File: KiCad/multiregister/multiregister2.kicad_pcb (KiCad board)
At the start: 2 copper layers, 6 parts, among them K1 CONN_3, K2 CONN_3, P1 CONN_5, P2 CONN_8, P3 CONN_5, U1 74HC595

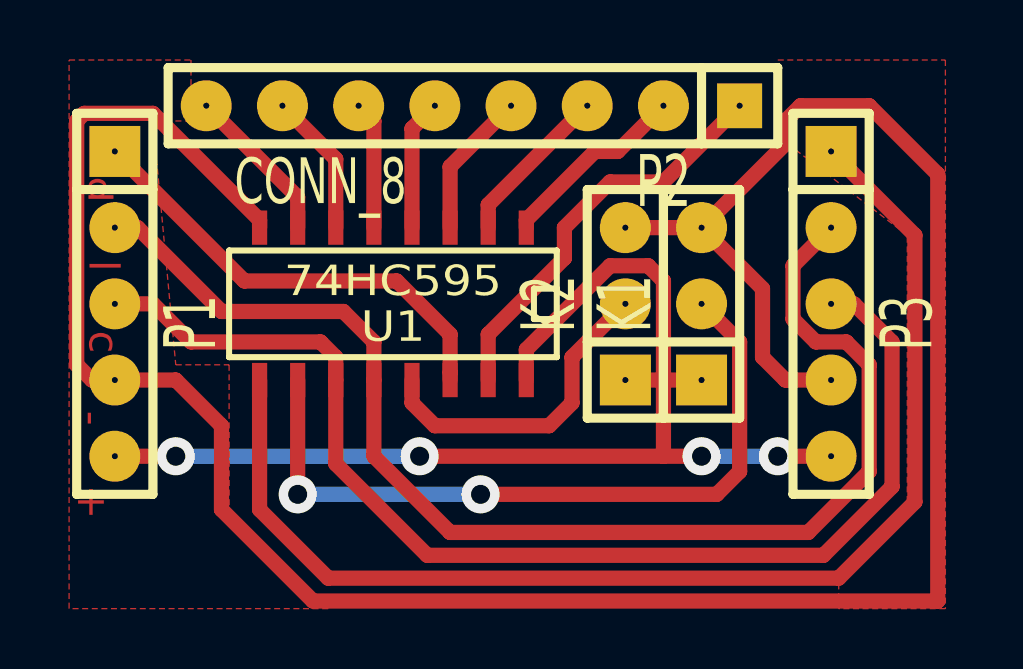
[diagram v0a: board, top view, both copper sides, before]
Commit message: multiregister: cases moved to the right side of the pcb
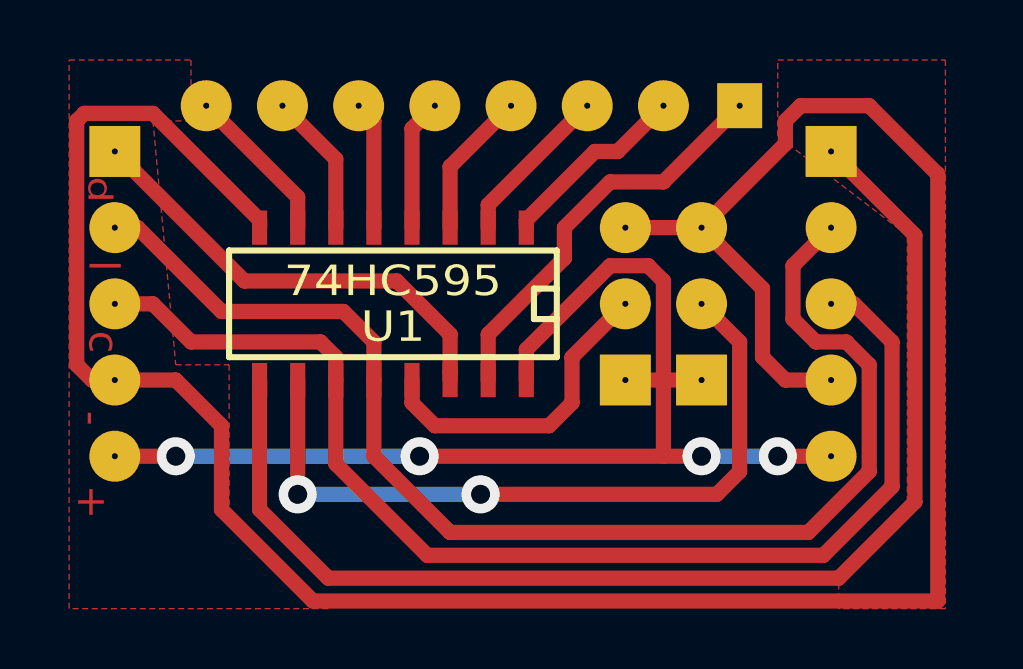
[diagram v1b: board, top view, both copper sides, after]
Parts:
- K1, K2, P1, P2, P3: moved to B.Cu
